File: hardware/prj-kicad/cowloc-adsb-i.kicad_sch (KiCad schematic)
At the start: 15 parts, among them U1 NSVG3117

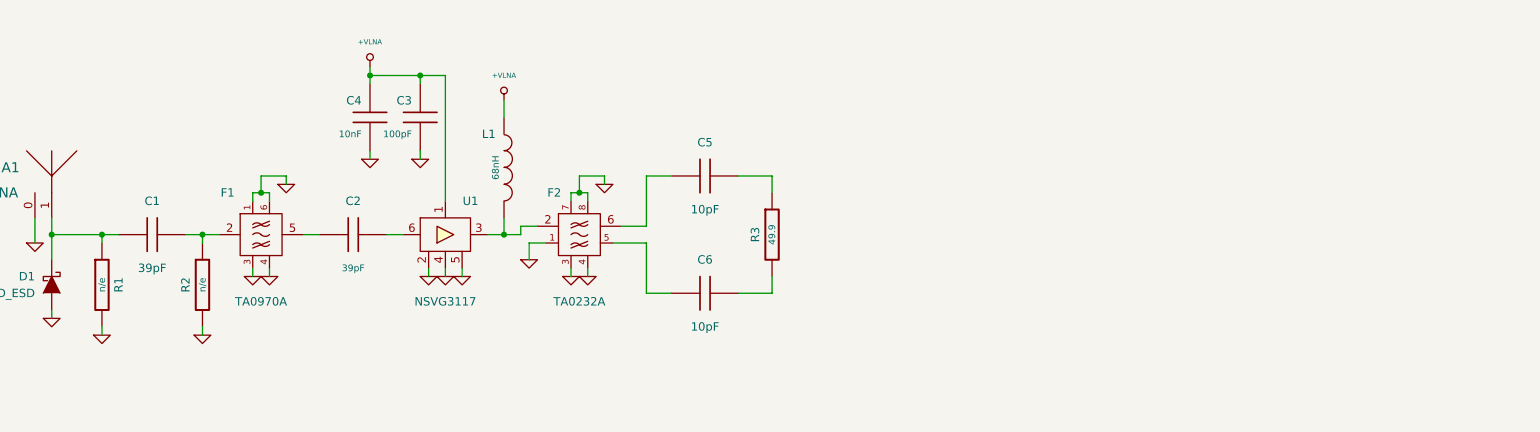
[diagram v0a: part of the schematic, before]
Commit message: = ADD: Insert a first signal detector based on AD8313
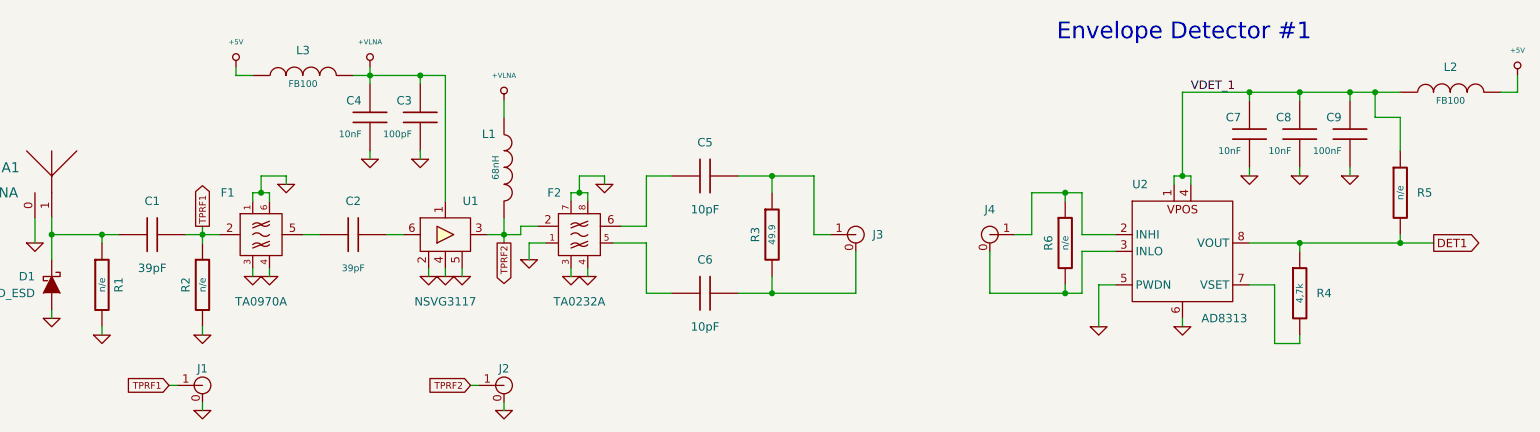
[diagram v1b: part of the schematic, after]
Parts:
- added C7, C8: 10nF, cowloc-adsb-i:SMD0603, symbol cowloc-adsb-i:C
- added C9: 100nF, cowloc-adsb-i:SMD0603, symbol cowloc-adsb-i:C
- added J1, J2, J3, J4: ~, cowloc-adsb-i:CONN_UFL-R-SMT-1, symbol cowloc-adsb-i:CONN_RF
- added L2, L3: FB100, cowloc-adsb-i:SMD0603, symbol cowloc-adsb-i:INDUCTOR
- added R4: 4,7k, cowloc-adsb-i:SMD0603, symbol cowloc-adsb-i:R
- added R5, R6: n/e, cowloc-adsb-i:SMD0603, symbol cowloc-adsb-i:R
- added U2: AD8313, cowloc-adsb-i:MSOP-8, symbol cowloc-adsb-i:AD8313
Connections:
- net +VLNA: now also L3.2
- net GND: now also C7.2, C8.2, C9.2, J1.0, J2.0, U2.5 (PWDN), U2.6
- net TPRF1: now reaches C1.2, F1.2, R2.1
- net TPRF1: now also J1.1
- net TPRF2: now reaches F2.2, L1.2, U1.3
- net TPRF2: now also J2.1
- net at C5.2, R3.1: now also J3.1
- net at C6.2, R3.2: now also J3.0
- new net: J4.0, R6.2, U2.3 (INLO)
- new net: J4.1, R6.1, U2.2 (INHI)
- new net: R4.2, U2.7 (VSET)
- new net +5V: L2.2, L3.1
- new net DET1: R4.1, R5.2, U2.8 (VOUT)
- new net VDET_1: C7.1, C8.1, C9.1, L2.1, R5.1, U2.1, U2.4
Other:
- note added: "Envelope Detector #1"

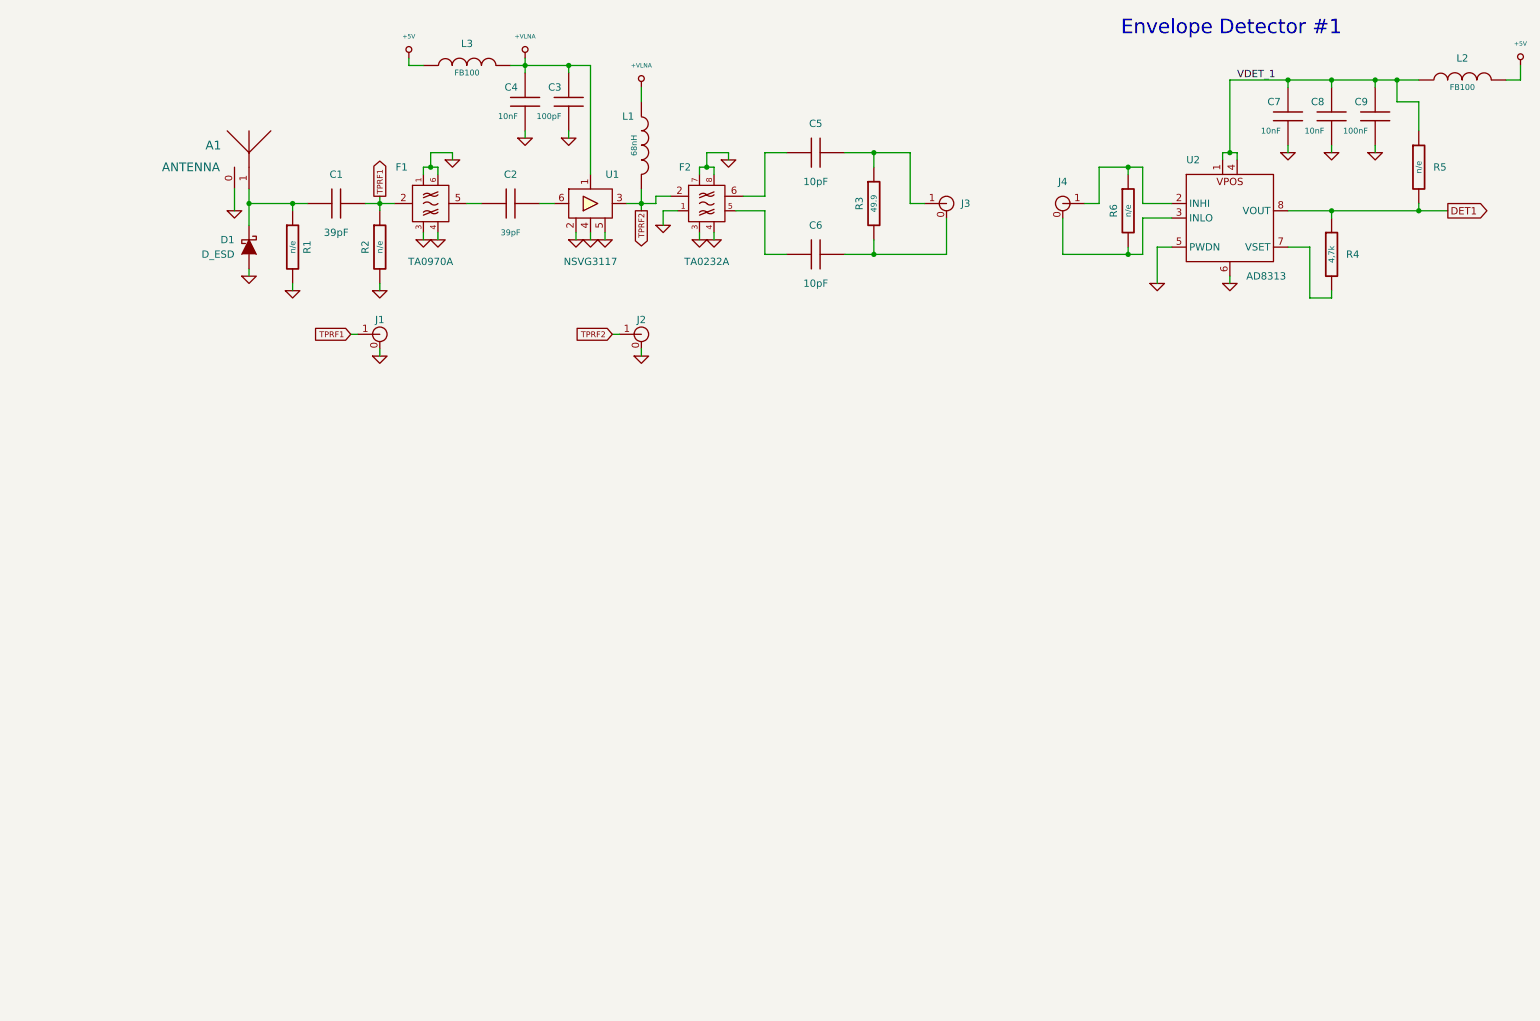
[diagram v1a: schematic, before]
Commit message: = ADD: Insert an alternate signal detector (AD993x) and a comparator on output
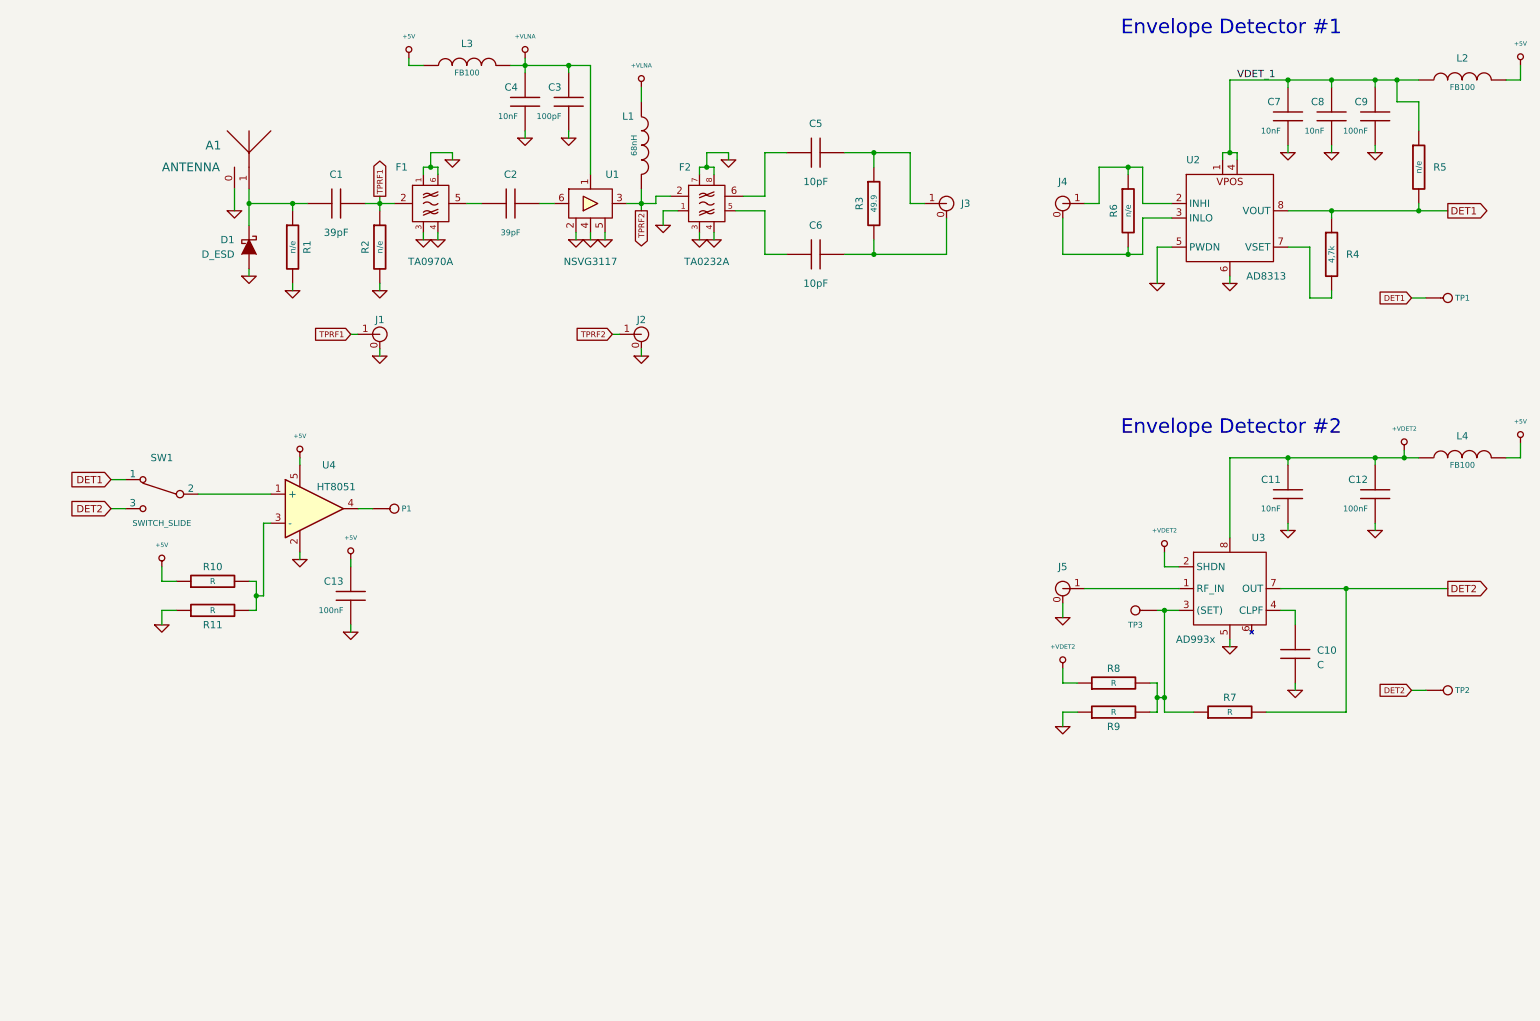
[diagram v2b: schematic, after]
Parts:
- added C10: C, cowloc-adsb-i:SMD0603, symbol cowloc-adsb-i:C
- added C11: 10nF, cowloc-adsb-i:SMD0603, symbol cowloc-adsb-i:C
- added C12, C13: 100nF, cowloc-adsb-i:SMD0603, symbol cowloc-adsb-i:C
- added J5: ~, cowloc-adsb-i:CONN_UFL-R-SMT-1, symbol cowloc-adsb-i:CONN_RF
- added L4: FB100, cowloc-adsb-i:SMD0603, symbol cowloc-adsb-i:INDUCTOR
- added P1, TP1, TP2, TP3: CONN_1, cowloc-adsb-i:TP_SMD, symbol cowloc-adsb-i:CONN_1
- added R10, R11, R7, R8, R9: R, cowloc-adsb-i:SMD0603, symbol cowloc-adsb-i:R
- added SW1: SWITCH_SLIDE, cowloc-adsb-i:SW_450301014042, symbol cowloc-adsb-i:SWITCH_SLIDE
- added U3: AD993x, cowloc-adsb-i:MSOP-8, symbol cowloc-adsb-i:AD993x
- added U4: HT8051, cowloc-adsb-i:SOT23-5, symbol cowloc-adsb-i:HT8051
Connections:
- net +5V: now also C13.1, L4.2, R10.1, U4.5
- net DET1: now also SW1.1, TP1.1
- net GND: now also C10.2, C11.2, C12.2, C13.2, J5.0, R11.1, R9.1, U3.5, U4.2
- new net: R7.1, R8.2, R9.2, TP3.1, U3.3 ((SET))
- new net: R10.2, R11.2, U4.3 (-)
- new net: SW1.2, U4.1 (+)
- new net: P1.1, U4.4
- new net: J5.1, U3.1 (RF_IN)
- new net: C10.1, U3.4 (CLPF)
- new net +VDET2: C11.1, C12.1, L4.1, R8.1, U3.2 (SHDN), U3.8
- new net DET2: R7.2, SW1.3, TP2.1, U3.7 (OUT)
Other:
- note added: "Envelope Detector #2"

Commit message: = ADD: Insert an hard-wired signal decoder (beta!!)
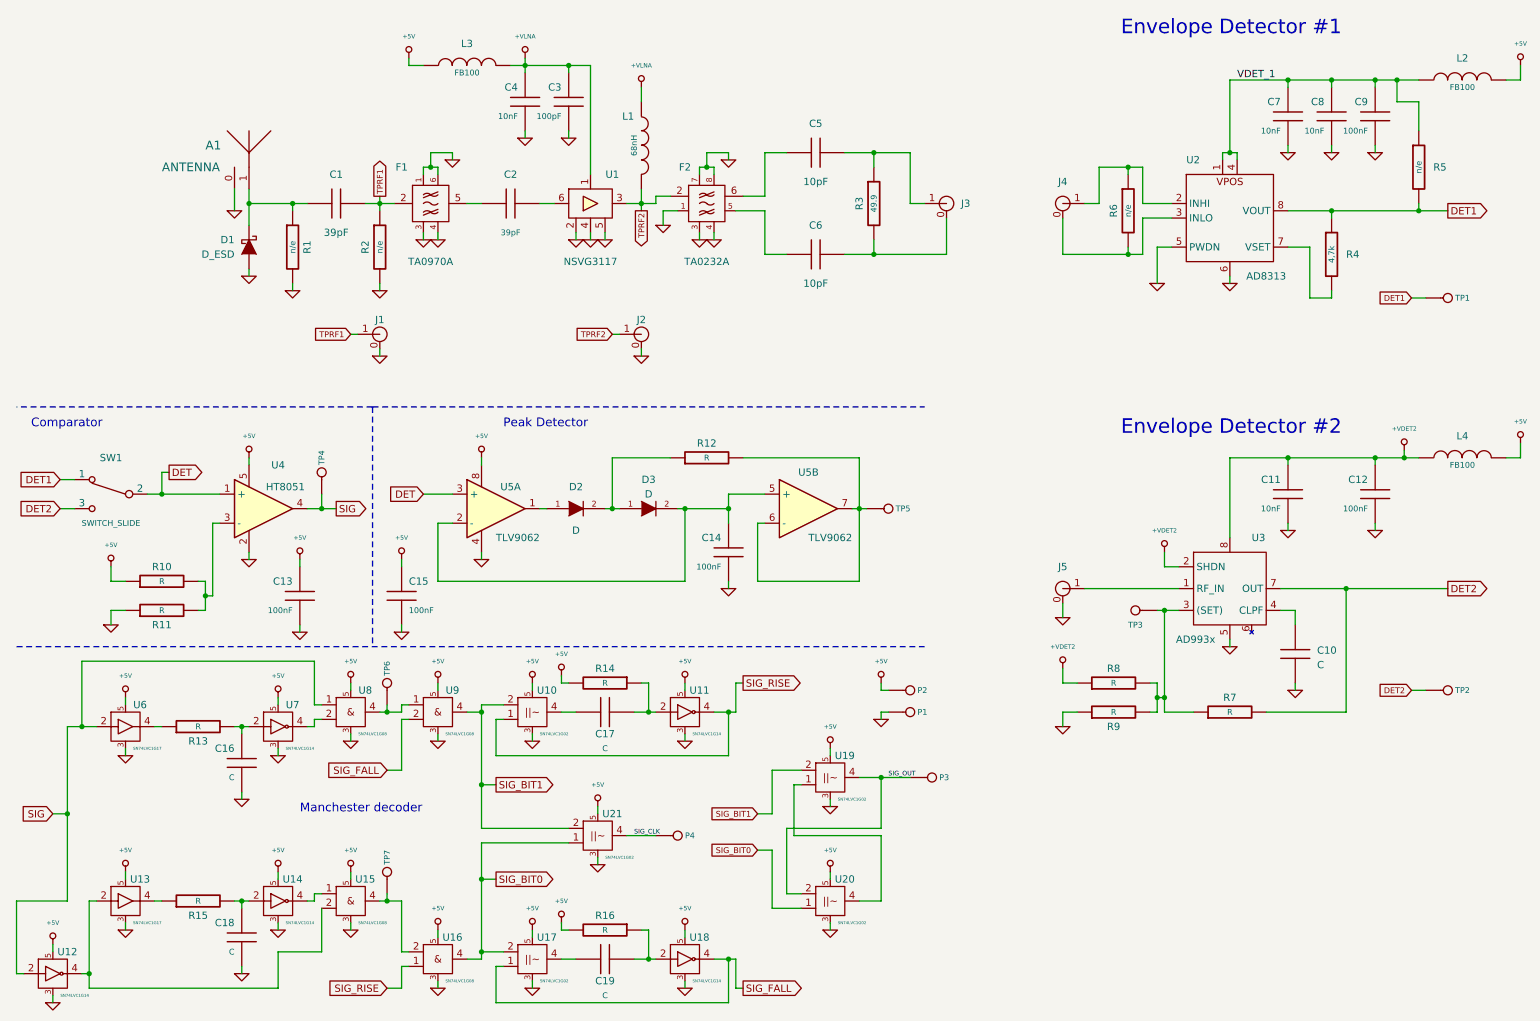
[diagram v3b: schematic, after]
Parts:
- added C14, C15: 100nF, cowloc-adsb-i:SMD0603, symbol cowloc-adsb-i:C
- added C16, C17, C18, C19: C, cowloc-adsb-i:SMD0603, symbol cowloc-adsb-i:C
- added D2, D3: D, cowloc-adsb-i:SOD-123, symbol cowloc-adsb-i:D
- added P1, P2, P3, P4: CONN_1, cowloc-adsb-i:TP_PIN, symbol cowloc-adsb-i:CONN_1
- added R12, R13, R14, R15, R16: R, cowloc-adsb-i:SMD0603, symbol cowloc-adsb-i:R
- added TP5, TP6, TP7: CONN_1, cowloc-adsb-i:TP_SMD, symbol cowloc-adsb-i:CONN_1
- added U10, U17, U19, U20, U21: SN74LVC1G02, cowloc-adsb-i:SOT23-5, symbol cowloc-adsb-i:SN74LVC1G02
- added U11, U12, U14, U18, U7: SN74LVC1G14, cowloc-adsb-i:SOT23-5, symbol cowloc-adsb-i:SN74LVC1G14
- added U13, U6: SN74LVC1G17, cowloc-adsb-i:SOT23-5, symbol cowloc-adsb-i:SN74LVC1G17
- added U15, U16, U8, U9: SN74LVC1G08, cowloc-adsb-i:SOT23-5, symbol cowloc-adsb-i:SN74LVC1G08
- added U5: TLV9062, cowloc-adsb-i:SOIC-8, symbol cowloc-adsb-i:TLV9062
- renumbered P1 to TP4
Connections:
- net +5V: now also C15.1, P2.1, R14.2, R16.2, U10.5, U11.5, U12.5, U13.5, U14.5, U15.5, U16.5, U17.5, U18.5, U19.5, U20.5, U21.5, U5.8, U6.5, U7.5, U8.5, U9.5
- net GND: now also C14.2, C15.2, C16.2, C18.2, P1.1, U10.3, U11.3, U12.3, U13.3, U14.3, U15.3, U16.3, U17.3, U18.3, U19.3, U20.3, U21.3, U5.4, U6.3, U7.3, U8.3, U9.3
- net DET: now reaches SW1.2, U4.1 (+)
- net DET: now also U5.3 (+)
- net SIG: now reaches TP4.1, U4.4
- net SIG: now also U12.2 (A), U6.2 (A), U8.1 (B)
- new net: TP6.1, U8.4 (Y), U9.1 (B)
- new net: C16.1, R13.2, U7.2 (A)
- new net: U7.4 (Y), U8.2 (A)
- new net: C14.1, D3.2 (K), U5.2 (-), U5.5 (+)
- new net: C18.1, R15.2, U14.2 (A)
- new net: U14.4 (Y), U15.1 (B)
- new net: TP7.1, U15.4 (Y), U16.2 (A)
- new net: U12.4 (Y), U13.2 (A), U15.2 (A)
- new net: R15.1, U13.4 (Y)
- new net: C17.1, U10.4 (Y)
- new net: C17.2, R14.1, U11.2 (A)
- new net: D2.2 (K), D3.1 (A), R12.1
- new net: C19.2, R16.1, U18.2 (A)
- new net: U19.1 (B), U20.4 (Y)
- new net: R13.1, U6.4 (Y)
- new net: R12.2, TP5.1, U5.6 (-), U5.7
- new net: C19.1, U17.4 (Y)
- new net: D2.1 (A), U5.1
- new net SIG_BIT0: U16.4 (Y), U17.2 (A), U20.1 (B), U21.1 (B)
- new net SIG_BIT1: U10.2 (A), U19.2 (A), U21.2 (A), U9.4 (Y)
- new net SIG_CLK: P4.1, U21.4 (Y)
- new net SIG_FALL: U17.1 (B), U18.4 (Y), U9.2 (A)
- new net SIG_OUT: P3.1, U19.4 (Y), U20.2 (A)
- new net SIG_RISE: U10.1 (B), U11.4 (Y), U16.1 (B)
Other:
- note added: "Comparator"
- note added: "Manchester decoder"
- note added: "Peak Detector"
- moved on the sheet: C13, R10, R11, SW1, TP4, U4
